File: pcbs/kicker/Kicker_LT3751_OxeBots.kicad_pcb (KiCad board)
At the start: 2 copper layers, 117.9 x 140 mm, 114 parts, among them J1 XT30PW-F, J2 12V, J3 3.3V, J4 XT30PW-F, J5 I2C, J6 ST Link, Q1 IRFB4227, Q2 BC847, Q3 FQPF20N60, Q4 BC847, Q5 BSS138, Q6 BSS138, SW1 SW_Push, T1 DCT15EFD-U44S003, U1 LT3751, U2 HCPL-3120, U3 AQV454, U4 STM32F070F6Px, U5 LM358, U6 HCNR201, U7 TLV9002

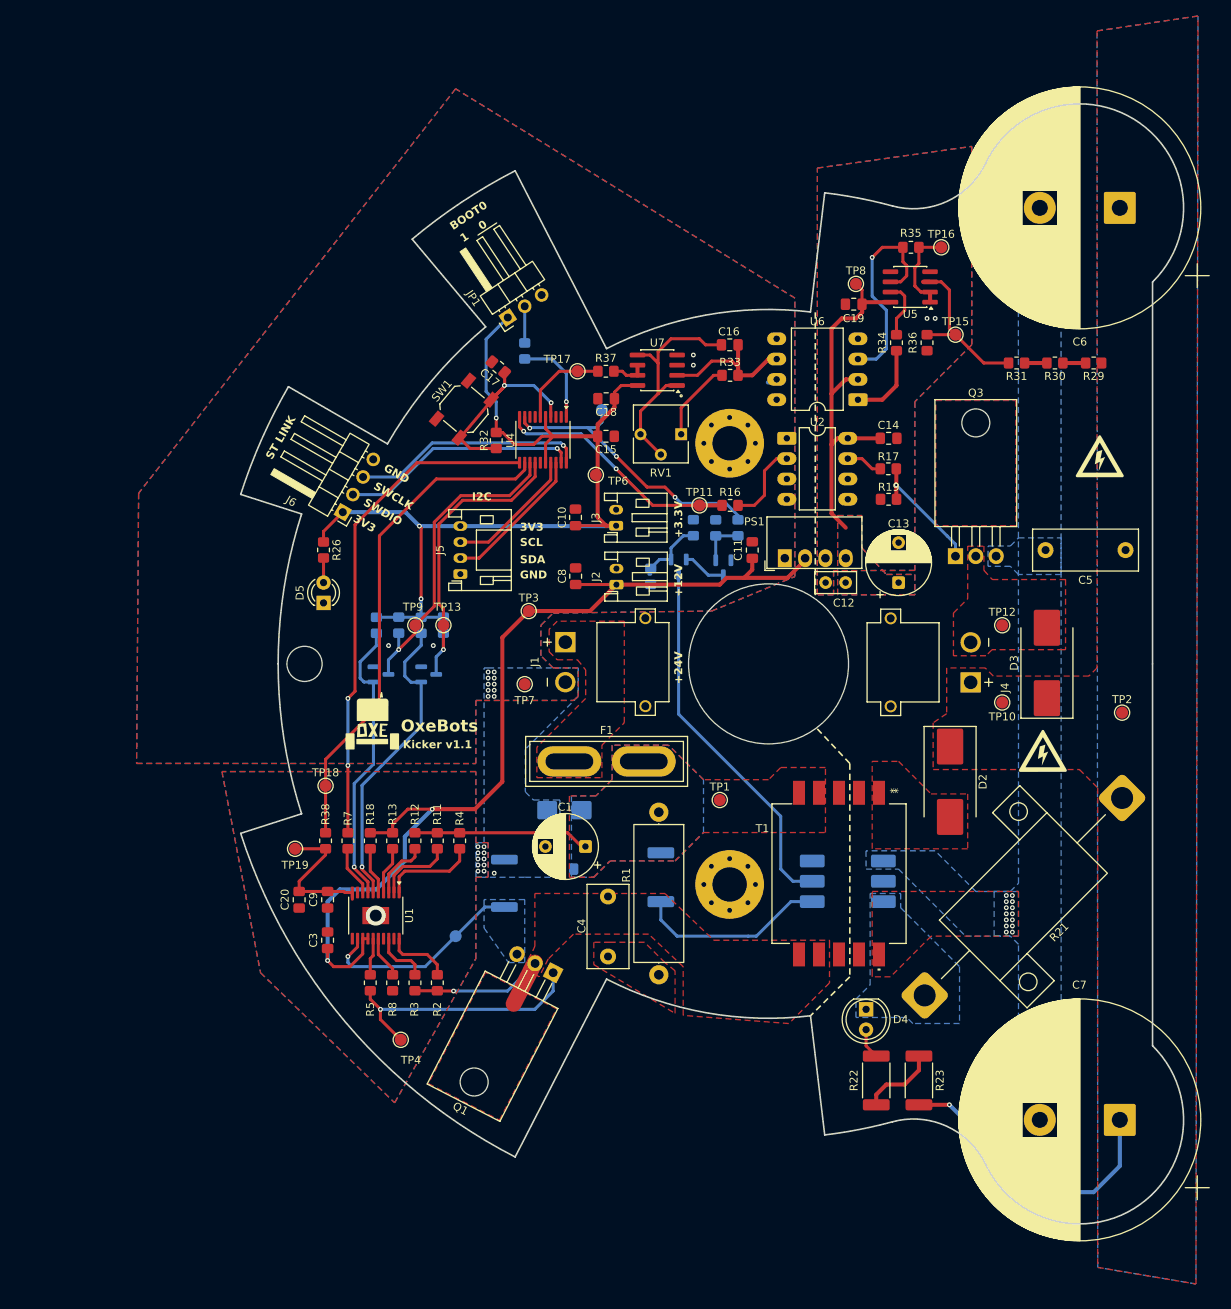
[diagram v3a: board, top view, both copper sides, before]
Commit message: Replaced MCU
Replaced MCU STM32F070F6P6 with STM32G031F6P6
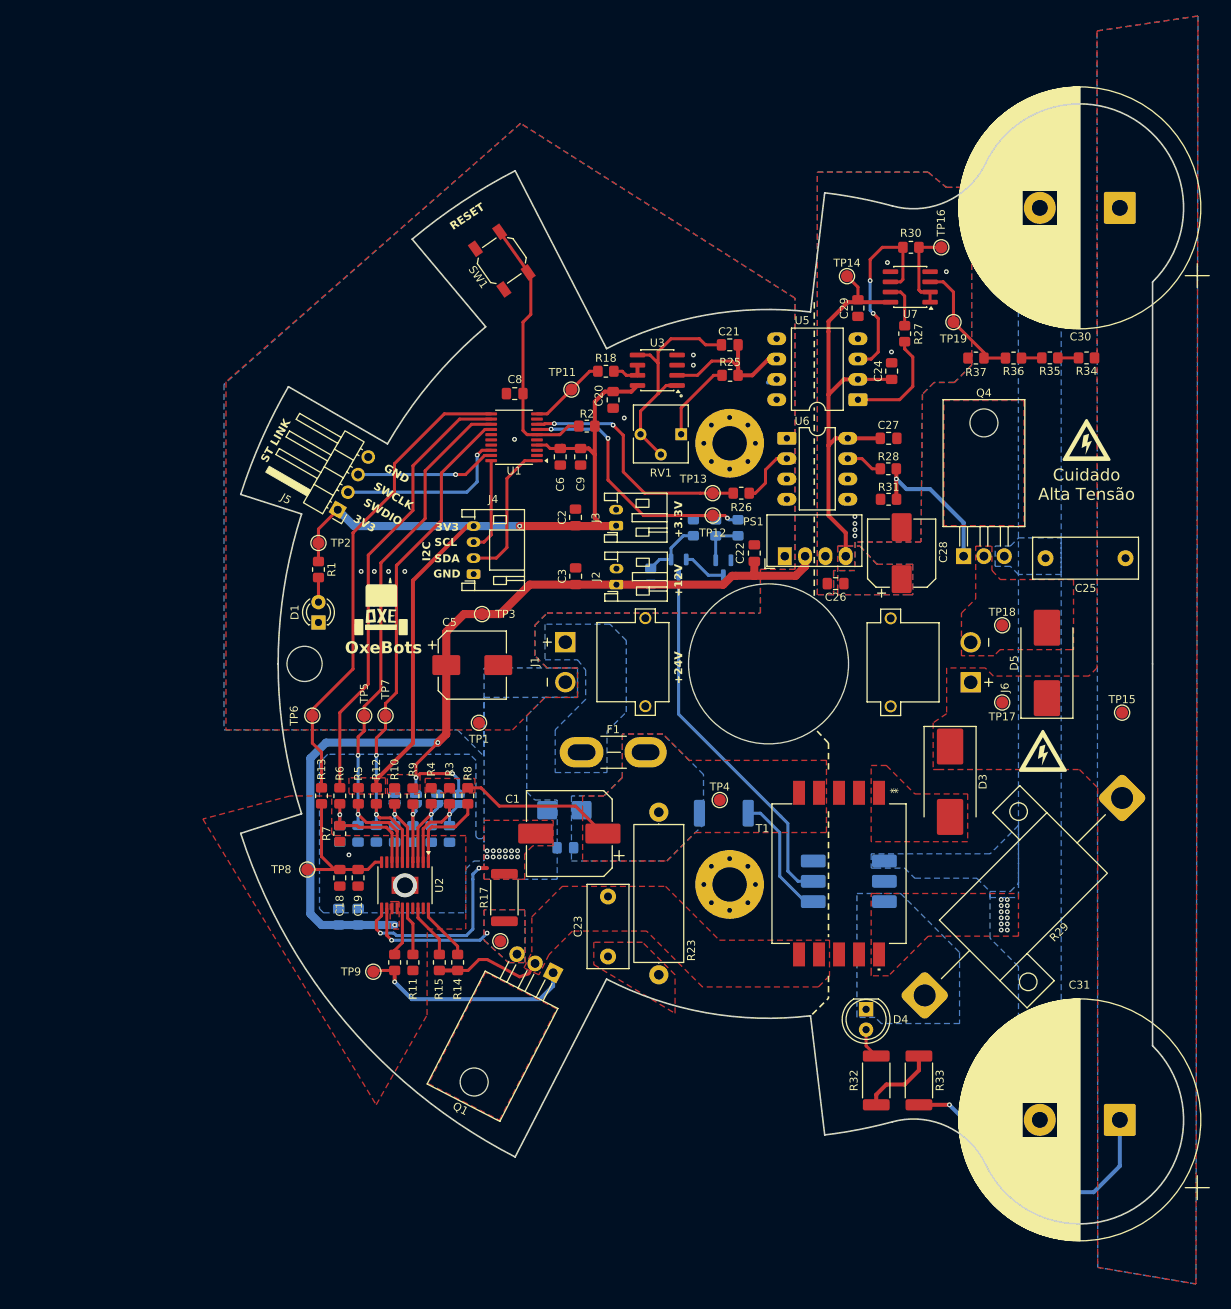
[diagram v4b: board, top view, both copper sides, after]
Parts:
- removed the Q2 at (55.8, 103.0)
- removed the Q4 at (61.7, 103.0)
- removed the R10 at (58.0, 96.9)
- removed the R14 at (60.8, 96.9)
- removed the R15 at (63.6, 96.9)
- removed R39: 10k, Resistor_SMD:R_0805_2012Metric_Pad1.20x1.40mm_HandSolder
- removed the R9 at (55.2, 96.9)
- removed the TP13 at (63.6, 96.9)
- removed the TP9 at (60.1, 96.9)
- removed the U4 at (76.0, 73.7)
- added C10: 100nF, Capacitor_SMD:C_0805_2012Metric_Pad1.18x1.45mm_HandSolder, B.Cu at (52.9, 133.3)
- added C11: 1nF, Capacitor_SMD:C_0805_2012Metric_Pad1.18x1.45mm_HandSolder, B.Cu at (64.3, 123.0)
- added C12: 1nF, Capacitor_SMD:C_0805_2012Metric_Pad1.18x1.45mm_HandSolder, B.Cu at (62.1, 123.0)
- added C14: 1nF, Capacitor_SMD:C_0805_2012Metric_Pad1.18x1.45mm_HandSolder, B.Cu at (50.6, 123.0)
- added C15: 1nF, Capacitor_SMD:C_0805_2012Metric_Pad1.18x1.45mm_HandSolder, B.Cu at (59.8, 123.0)
- added C16: 1nF, Capacitor_SMD:C_0805_2012Metric_Pad1.18x1.45mm_HandSolder, B.Cu at (57.5, 123.0)
- added C17: 1nF, Capacitor_SMD:C_0805_2012Metric_Pad1.18x1.45mm_HandSolder, B.Cu at (55.2, 123.0)
- added C24: 100nF, Capacitor_SMD:C_0805_2012Metric_Pad1.18x1.45mm_HandSolder, F.Cu at (119.6, 65.1)
- added C28: 470uF, Capacitor_SMD:CP_Elec_8x10, F.Cu at (120.9, 87.9)
- added C5: 470uF, Capacitor_SMD:CP_Elec_8x10, F.Cu at (67.2, 101.9)
- added C9: 10uF, Capacitor_SMD:C_0805_2012Metric_Pad1.18x1.45mm_HandSolder, F.Cu at (80.7, 75.8)
- added JP2: OVLO1_BYPASS, Jumper:SolderJumper-2_P1.3mm_Open_RoundedPad1.0x1.5mm, B.Cu at (62.8, 118.6)
- added JP3: UVLO2_BYPASS, Jumper:SolderJumper-2_P1.3mm_Open_RoundedPad1.0x1.5mm, B.Cu at (60.2, 118.6)
- added JP4: OVLO2_BYPASS, Jumper:SolderJumper-2_P1.3mm_Open_RoundedPad1.0x1.5mm, B.Cu at (57.5, 118.6)
- added NT1: NetTie_2, NetTie:NetTie-2_SMD_Pad0.5mm, F.Cu at (68.5, 127.3)
- added R12: 100k, Resistor_SMD:R_0805_2012Metric_Pad1.20x1.40mm_HandSolder, F.Cu at (55.2, 118.2)
- added R5: 100k, Resistor_SMD:R_0805_2012Metric_Pad1.20x1.40mm_HandSolder, F.Cu at (52.9, 118.2)
- added R7: 10k, Resistor_SMD:R_0805_2012Metric_Pad1.20x1.40mm_HandSolder, F.Cu at (50.6, 122.9)
- added TP5: DONE, TestPoint:TestPoint_Pad_D1.5mm, F.Cu at (53.7, 108.2)
- added TP7: FAULT, TestPoint:TestPoint_Pad_D1.5mm, F.Cu at (56.3, 108.2)
- added U1: STM32G031F6Px, Package_SO:TSSOP-20_4.4x6.5mm_P0.65mm, F.Cu at (72.4, 73.4)
- C1: value 1000uF -> 470uF; footprint Capacitor_THT:CP_Radial_D8.0mm_P5.00mm -> Capacitor_SMD:CP_Elec_10x12.5
- C13: value 220uF -> 1nF; footprint Capacitor_THT:CP_Radial_D8.0mm_P5.00mm -> Capacitor_SMD:C_0805_2012Metric_Pad1.18x1.45mm_HandSolder; moved to B.Cu
- C26: renamed from C12; footprint Capacitor_THT:C_Disc_D5.0mm_W2.5mm_P2.50mm -> Capacitor_SMD:C_0805_2012Metric_Pad1.18x1.45mm_HandSolder
- C7: renamed from C3; value 100nF -> 10uF; moved to B.Cu
- F1: footprint Fuse:Fuse_Blade_ATO_directSolder -> Fuse:Fuse_Blade_Mini_directSolder
- JP1: value Boot0 -> UVLO1_BYPASS; footprint Connector_PinHeader_2.54mm:PinHeader_1x03_P2.54mm_Horizontal -> Jumper:SolderJumper-2_P1.3mm_Open_RoundedPad1.0x1.5mm; moved to B.Cu
- PS1: value B1215S -> Converter_DC-DC_BxxxxS 1W
- R11: renamed from R8; value 1,8K -> 1,8K (NOTA 3)
- R13: renamed from R38; value 10k -> 4.7k
- R17: renamed from R6; value 25m (NOTA 1) -> 25m (NOTA 2); moved to F.Cu
- R23: renamed from R1; value 4,7K -> 47R 5W
- R25: renamed from R33; value 47k -> 51k
- RV1: value 20k -> 10k
- TP10: renamed from TP5; moved to F.Cu
- TP12: renamed from TP14; moved to F.Cu
- U2: renamed from U1; footprint Package_SO:TSSOP-20-1EP_4.4x6.5mm_P0.65mm_EP2.15x3.35mm -> oxebots:LT3751
- U4: renamed from U3; footprint Package_DIP:DIP-6_W8.89mm_SMDSocket_LongPads -> oxebots:AQV454
- moved C13 74.5 mm to (52.9, 123.0), turned to -90 degrees
- moved JP1 60.5 mm to (65.5, 118.6), turned to -90 degrees
- moved G*** 49.9 mm to (143.5, 68.7)
- moved TP2 35.7 mm to (48.0, 86.6)
- moved SW1 19.2 mm to (70.9, 51.3), turned to 125 degrees
- moved TP12 19.1 mm to (97.2, 83.2), turned to 0 degrees
- moved G*** 14.3 mm to (55.7, 95.0)
- moved R2 11.5 mm to (81.5, 72.0), turned to 180 degrees
- moved R24 11.2 mm to (98.6, 120.4), turned to 0 degrees
- moved TP9 9.17 mm to (54.8, 140.2)
- moved TP6 8.92 mm to (47.2, 108.2)
- moved TP1 7.48 mm to (68.0, 109.1)
- moved R37 6.41 mm to (130.2, 63.5), turned to 180 degrees
- moved R10 6.38 mm to (57.5, 118.2)
- moved C6 6.26 mm to (78.2, 75.8), turned to -90 degrees
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- renumbered C20 to C18, C9 to C19, C10 to C2, C18 to C20, C16 to C21, C11 to C22, C4 to C23, C5 to C25, C14 to C27, C19 to C29, C8 to C3, C6 to C30, C7 to C31, C2 to C4, C15 to C6, C17 to C8, D5 to D1, D1 to D2, D2 to D3, D3 to D5, J5 to J4, J6 to J5, J4 to J6, Q5 to Q2, Q6 to Q3, Q3 to Q4, R26 to R1, R18 to R10, R2 to R14, R3 to R15, R5 to R16, R37 to R18, R24 to R19, R32 to R2, R27 to R20, R25 to R21, R28 to R22, R20 to R24, R16 to R26, R34 to R27, R17 to R28, R21 to R29, R11 to R3, R35 to R30, R19 to R31, R22 to R32, R23 to R33, R29 to R34, R30 to R35, R31 to R36, R36 to R37, R12 to R4, R7 to R6, R4 to R8, R13 to R9, TP7 to TP1, TP17 to TP11, TP11 to TP13, TP8 to TP14, TP2 to TP15, TP10 to TP17, TP12 to TP18, TP15 to TP19, TP6 to TP2, TP1 to TP4, TP18 to TP6, TP19 to TP8, TP4 to TP9, U7 to U3, U6 to U5, U2 to U6, U5 to U7
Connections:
- C13 pad 1: +15V_SEC -> LT3751_DONE
- C13 pad 2: GNDPWR -> GND
- JP1 pad 1: +3.3V -> +12V
- JP1 pad 2: Net-(JP1-C) -> LT3751_UVLO_1
- U2 pad 11: GND -> Net-(U2-CSN)
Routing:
- net MCU_IN_DONE: track 40.1 -> 0.00 mm, vias 1 -> 0
- net MCU_IN_FAULT: track 37.7 -> 0.00 mm, vias 1 -> 0
- net LT3751_DONE: track 36.3 -> 69.4 mm, vias 1 -> 2
- net LT3751_FAULT: track 38.5 -> 65.3 mm, vias 1 -> 2
- net Net-(U2-CSN): track 0.00 -> 23.5 mm, vias 0 -> 2
- net +3.3V: track 124.4 -> 111.4 mm, vias 3 -> 1
- net MCU_STLINK_SWCLK: track 29.2 -> 17.6 mm
- net MCU_BOOT0: track 11.4 -> 0.00 mm, vias 1 -> 0
- net Net-(Q1-S): track 26.3 -> 16.5 mm, vias 1 -> 2
- net +15V_SEC: track 48.4 -> 58.0 mm
- net Net-(Q1-D): track 16.5 -> 6.91 mm, vias 1 -> 0
- net +12V: track 128.6 -> 137.7 mm, vias 2 -> 4
- net Net-(U2-CHARGE): track 6.27 -> 14.7 mm, vias 0 -> 1
- net Net-(R24-Pad2): track 23.8 -> 15.8 mm
- net MCU_STLINK_SWDIO: track 29.9 -> 22.0 mm
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- added copper zone on F.Cu, net +12V
- added copper zone on F.Cu, net +3.3V
- added copper zone on B.Cu, net Net-(F1-Pad1)
- added copper zone on F.Cu, net Net-(Q1-S)
- removed copper zone on F.Cu, net Net-(F1-Pad1)
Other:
- board text added: "RESET"
- board text removed: "0"
- board text removed: "1"
- board text removed: "BOOT0"
- board text removed: "Kicker v1.1"

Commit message: Update FB low pass filter
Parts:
- added C32: 10nF, Capacitor_SMD:C_0805_2012Metric_Pad1.18x1.45mm_HandSolder, F.Cu at (50.6, 128.4)
- added R38: 10k, Resistor_SMD:R_0805_2012Metric_Pad1.20x1.40mm_HandSolder, F.Cu at (48.3, 122.9)
- R13: value 4.7k -> 1k
- moved C18 6.36 mm to (45.8, 124.3)
- moved TP8 1.77 mm to (47.3, 129.0)
- moved C19 0.05 mm to (52.9, 128.4)
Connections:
- C18 pad 1: LT3751_FB -> Net-(C18-Pad1)
- R13 pad 2: LT3751_FB -> Net-(C18-Pad1)
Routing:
- net Net-(C18-Pad1): track 0.00 -> 5.81 mm
- net LT3751_FB: track 19.2 -> 13.6 mm
- net GND: vias 22 -> 21
